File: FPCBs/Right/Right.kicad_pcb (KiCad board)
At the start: 2 copper layers, 61.5 x 89.2 mm, 23 parts, among them J1 PCB, J5 2nd Focus+Shutter, J6 Conn_01x03_Pin, SW1 Mode Dial, SW2 ON/OFF, SW3 Focus+Shutter, SW4 Focus+Shutter, SW6 ON/OFF, U1 SG-105, U2 SG-105

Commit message: Fixes to the right pcb
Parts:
- removed SW6: ON/OFF, Leica-G9ii:Switch_Detection_Bidirectional
- moved J5 22.3 mm to (135.2, 144.9)
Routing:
- net Net-(J1-Pin_5): track 126.0 -> 96.1 mm, vias 2 -> 1
- net Net-(J1-Pin_26): track 97.9 -> 77.2 mm
- net Net-(J1-Pin_7): track 116.1 -> 95.9 mm, vias 2 -> 1
- net Net-(J1-Pin_25): track 98.2 -> 82.9 mm
- net Net-(J1-Pin_23): track 112.5 -> 100.1 mm, vias 4 -> 3
- net Net-(J1-Pin_33): track 92.2 -> 99.7 mm
- net Net-(J1-Pin_34): track 89.7 -> 97.1 mm
- net Net-(J1-Pin_35): track 86.2 -> 93.6 mm
- net Net-(D2-A): track 83.4 -> 84.1 mm
- net Net-(D2-K): track 89.3 -> 89.8 mm
- added copper zone on F.Cu, net (none)
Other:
- outline, holes or cut-outs redrawn

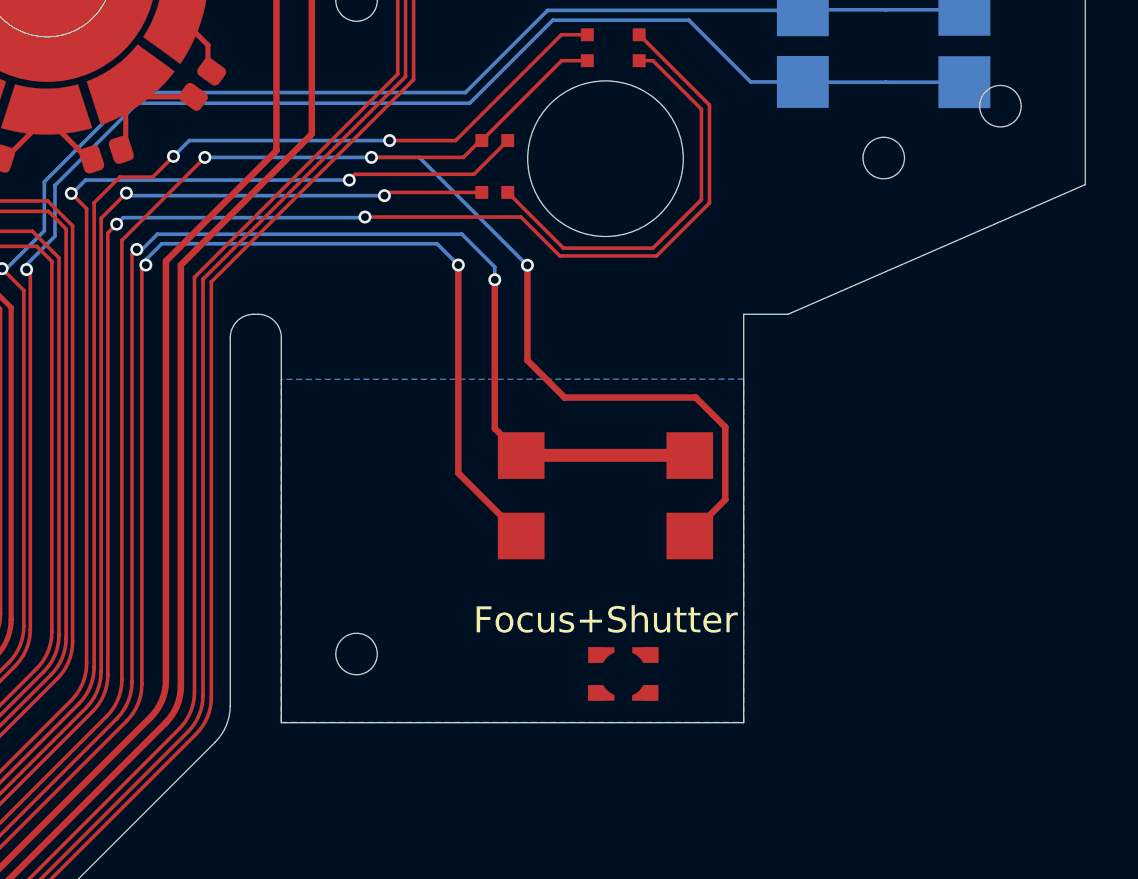
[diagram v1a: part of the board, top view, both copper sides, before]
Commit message: Add serpentines
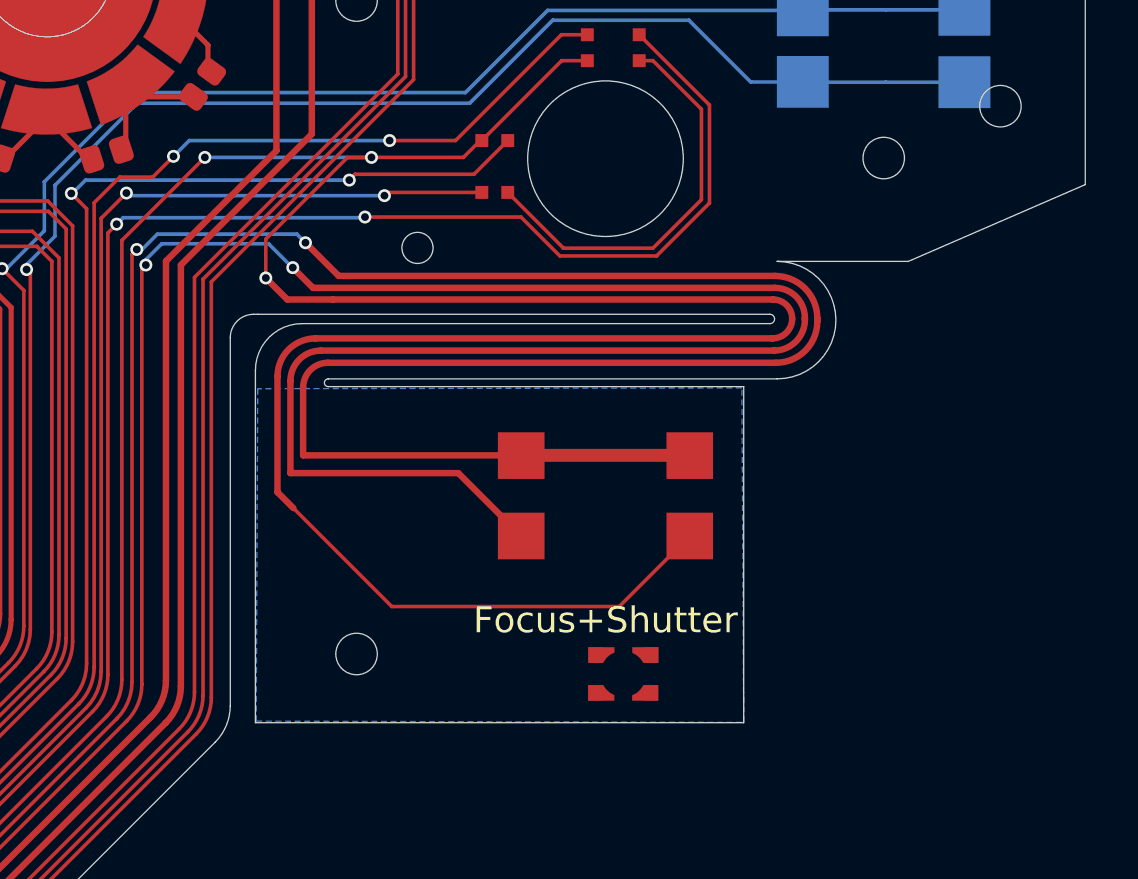
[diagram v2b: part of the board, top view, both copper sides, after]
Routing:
- net Net-(J1-Pin_23): track 100.1 -> 147.4 mm
- net Net-(J1-Pin_25): track 82.9 -> 121.0 mm
- net Net-(J1-Pin_26): track 77.2 -> 114.7 mm
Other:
- outline, holes or cut-outs redrawn

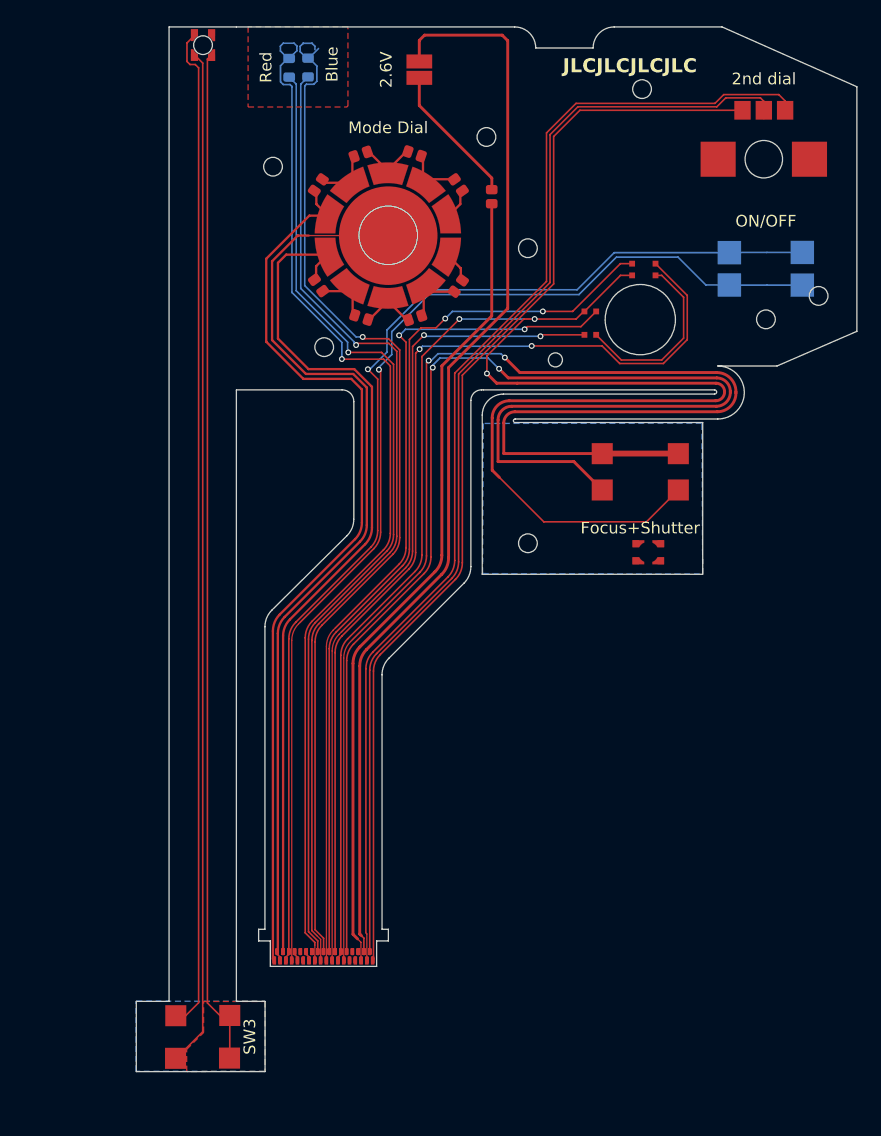
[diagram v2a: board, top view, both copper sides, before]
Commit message: Add through holes for on off switch
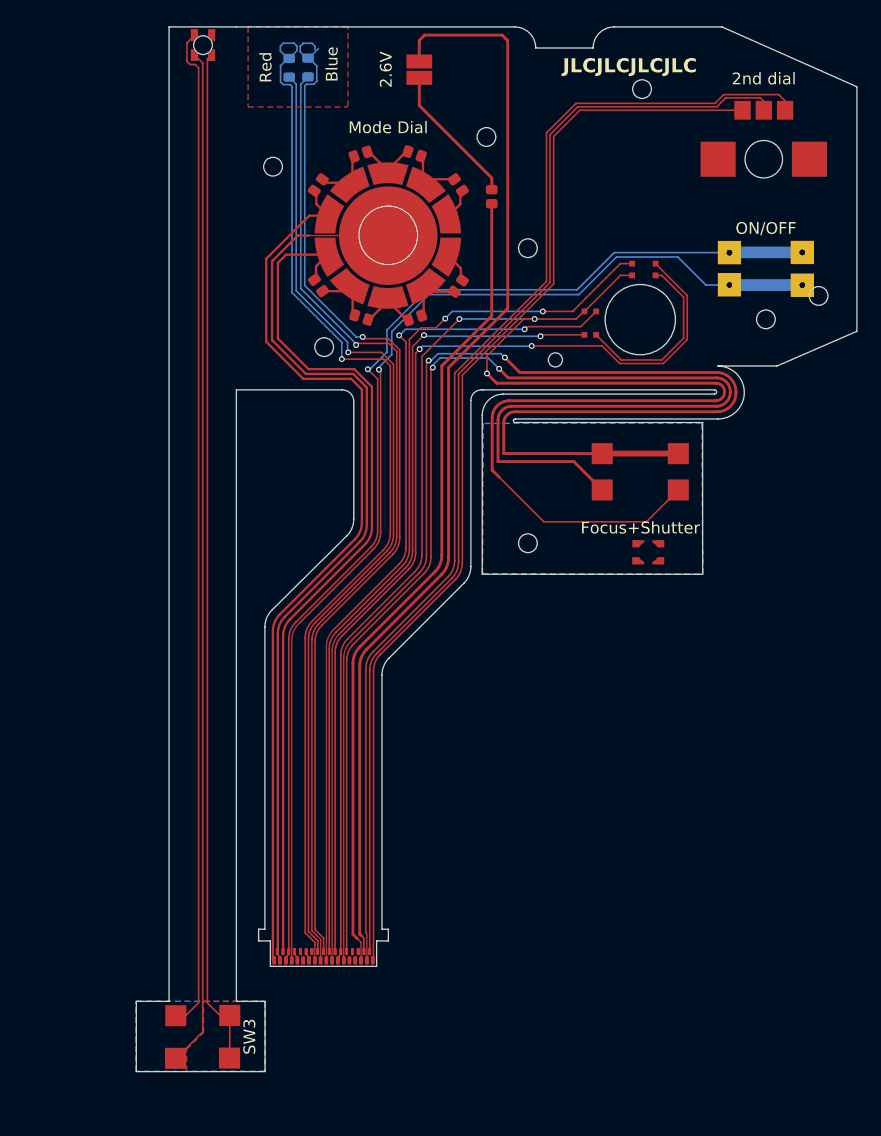
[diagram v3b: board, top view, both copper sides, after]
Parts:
- SW2: footprint Leica-G9ii:Switch_Detection_Bidirectional -> Leica-G9ii:Switch_ON_OFF

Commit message: Fix small battery footprint
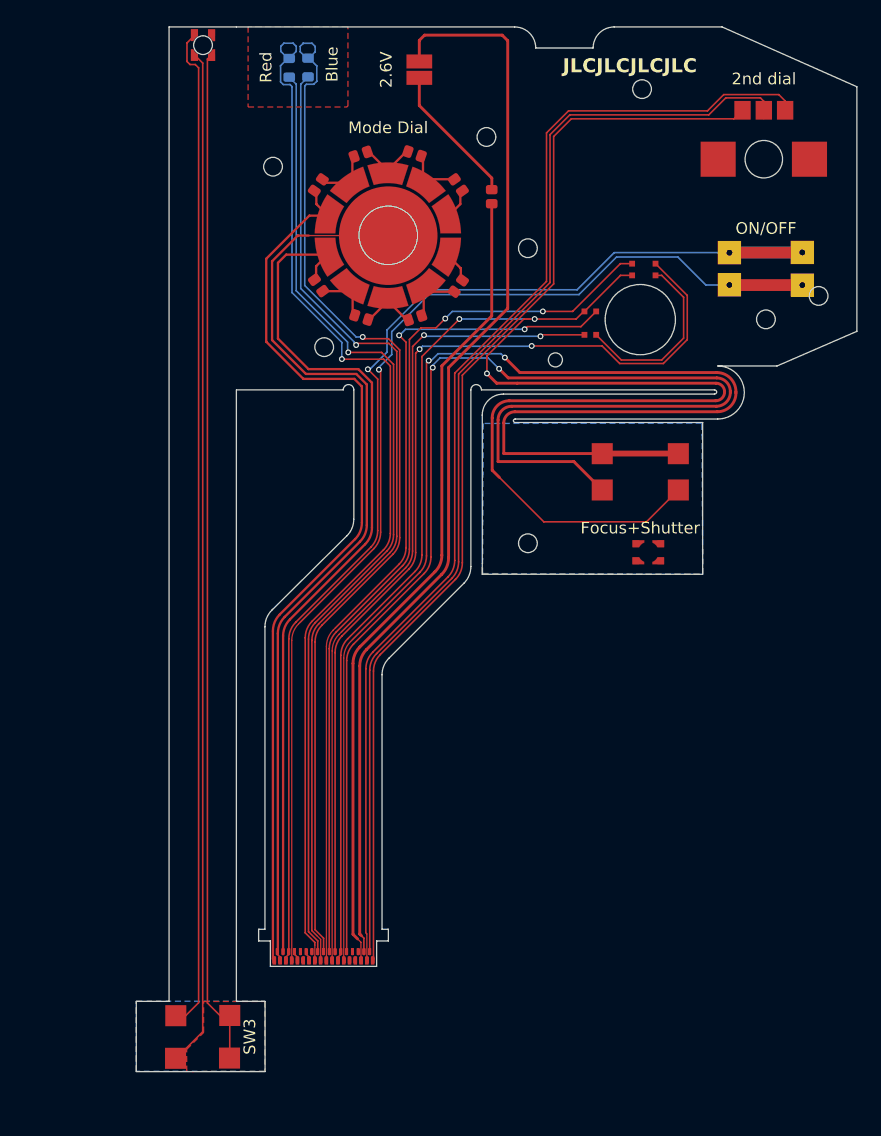
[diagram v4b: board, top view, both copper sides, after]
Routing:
- net Net-(J1-Pin_5): track 96.2 -> 102.4 mm
- net Net-(J1-Pin_7): track 96.0 -> 102.2 mm
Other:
- outline, holes or cut-outs redrawn

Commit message: Fixes on the shutter
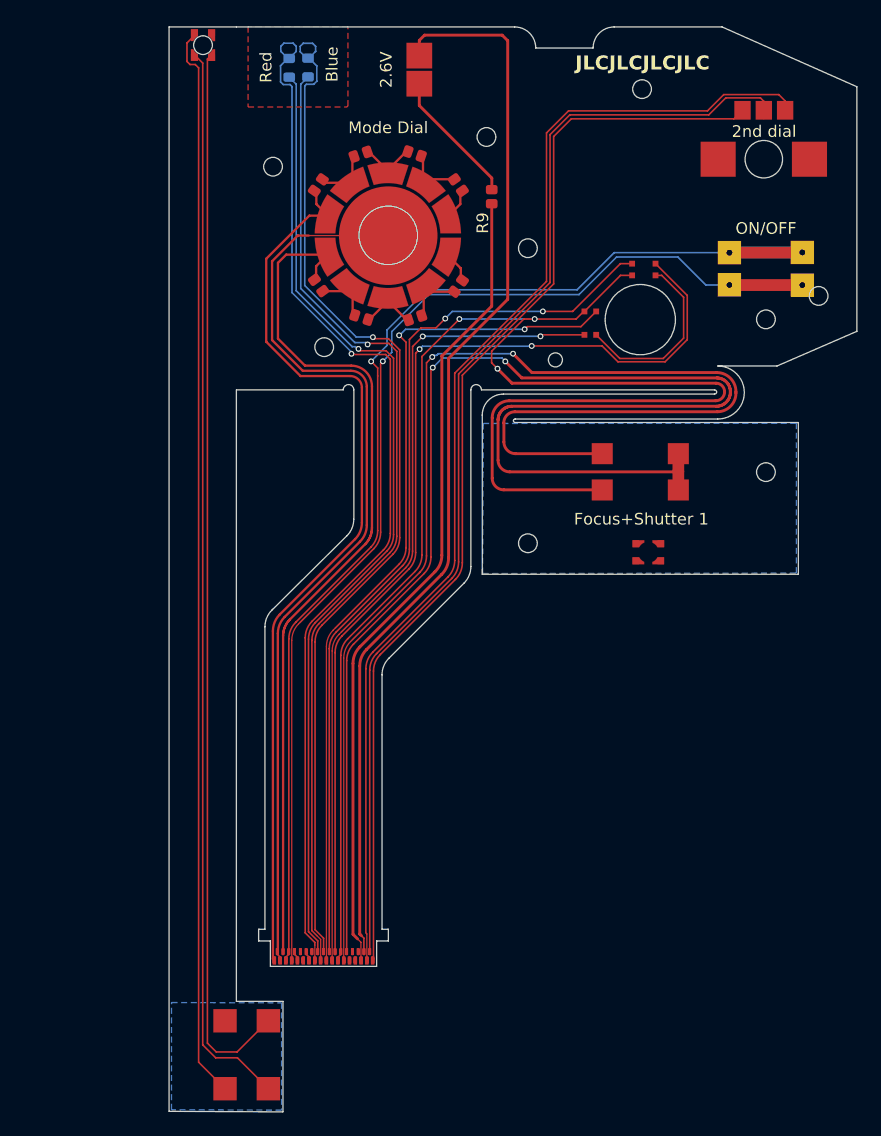
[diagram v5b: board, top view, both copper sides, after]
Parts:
- SW3: value Focus+Shutter -> Focus+Shutter 1; footprint Leica-G9ii:Switch_Shutter_Olympus -> Leica-G9ii:Shutter_Canon
- SW4: value Focus+Shutter -> Focus+Shutter 2; footprint Leica-G9ii:Switch_Shutter_Canon -> Leica-G9ii:Shutter_Olympus
- moved SW3 61.0 mm to (134.5, 138.0), turned to 0 degrees
- moved SW4 60.1 mm to (100.9, 187.8)
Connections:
- J5 pad 1: Net-(J1-Pin_26) -> Net-(J1-Pin_23)
- J5 pad 2: Net-(J1-Pin_23) -> Net-(J1-Pin_26)
- SW3 pad 1: Net-(J6-Pin_2) -> Net-(J1-Pin_23)
- SW3 pad 2: Net-(J6-Pin_1) -> Net-(J1-Pin_26)
- SW3 pad 3: Net-(J6-Pin_3) -> Net-(J1-Pin_26)
- SW4 pad 1: Net-(J1-Pin_26) -> Net-(J6-Pin_1)
- SW4 pad 2: Net-(J1-Pin_23) -> Net-(J6-Pin_2)
- SW4 pad 3: Net-(J1-Pin_25) -> Net-(J6-Pin_2)
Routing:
- net Net-(J1-Pin_23): track 147.4 -> 138.1 mm
- net Net-(J1-Pin_26): track 114.7 -> 123.7 mm
- net Net-(J1-Pin_25): track 121.0 -> 113.9 mm
- net Net-(J6-Pin_1): track 86.0 -> 91.6 mm
- net Net-(J6-Pin_2): track 87.0 -> 92.2 mm
- net Net-(J6-Pin_3): track 87.1 -> 91.4 mm
- net Net-(BT1--): track 92.7 -> 92.2 mm
- net Net-(BT1-+): track 12.2 -> 11.7 mm
- removed copper zone on F.Cu, net Net-(J6-Pin_3)
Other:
- board size 61.5 x 89.2 mm -> 58.8 x 92.7 mm

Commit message: Second shutter FPC
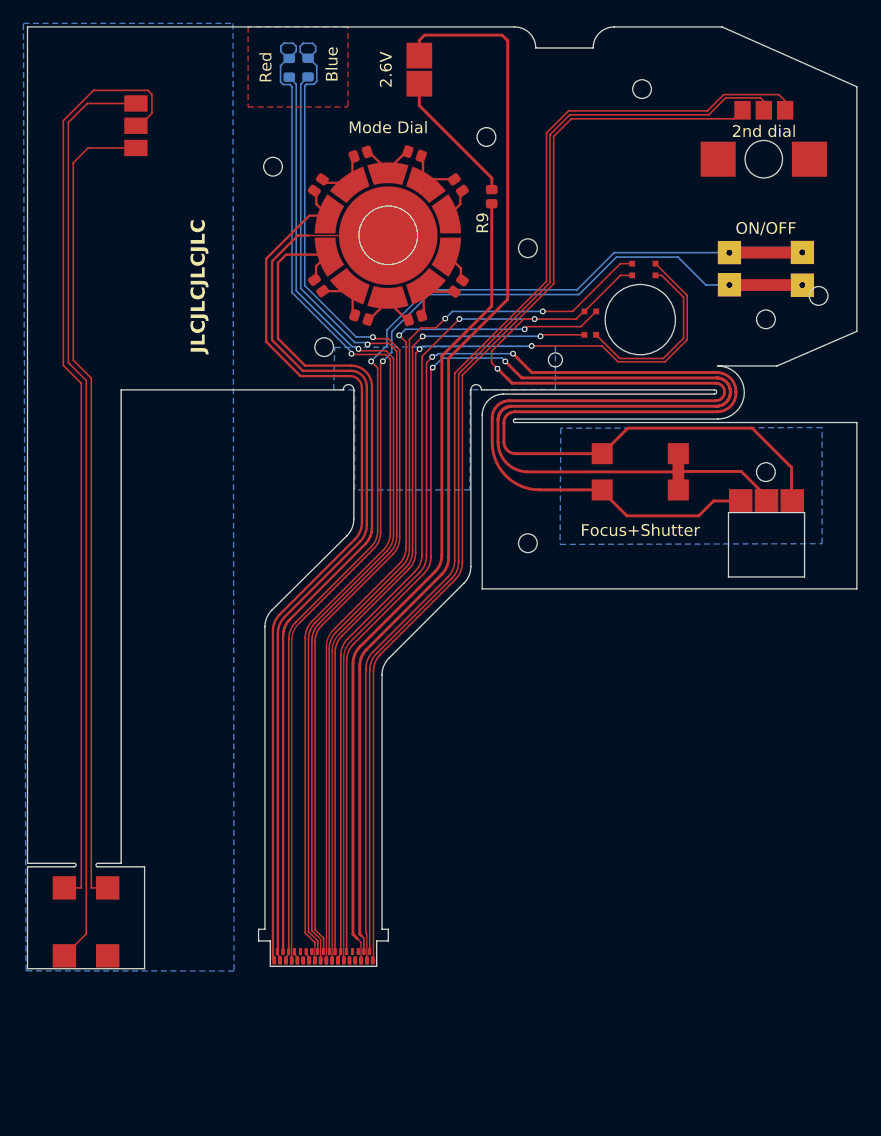
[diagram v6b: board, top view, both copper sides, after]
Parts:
- J5: footprint Leica-G9ii:Connector-4Pins -> Leica-G9ii:Connector-Springs-3Pins
- J6: value Conn_01x03_Pin -> FPC Focus/Shutter; footprint Leica-G9ii:Connector-4Pins -> Leica-G9ii:FPC-Springs-3Pins
- SW3: value Focus+Shutter 1 -> Focus+Shutter
- moved SW4 17.8 mm to (87.2, 176.4)
- moved J5 10.1 mm to (145.3, 144.2), turned to 0 degrees
- moved J6 8.96 mm to (91.4, 108.4), turned to -90 degrees
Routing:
- net Net-(J6-Pin_3): track 91.4 -> 69.5 mm
- net Net-(J1-Pin_25): track 113.9 -> 135.3 mm
- net Net-(J6-Pin_1): track 91.6 -> 78.9 mm
- net Net-(J6-Pin_2): track 92.2 -> 79.8 mm
- net Net-(J1-Pin_23): track 138.1 -> 150.3 mm
- net Net-(J1-Pin_26): track 123.7 -> 131.8 mm
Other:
- board size 58.8 x 92.7 mm -> 70.8 x 80.4 mm
